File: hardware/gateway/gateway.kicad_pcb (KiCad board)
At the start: 2 copper layers, 65 x 32 mm, 29 parts, among them J1 FTDI, J2 Conn_Coaxial, J3 Raspberry_Pi_2_3, U1 RFM69HW, U2 MCP7940N-xSN, Y1 32768 - 6pF

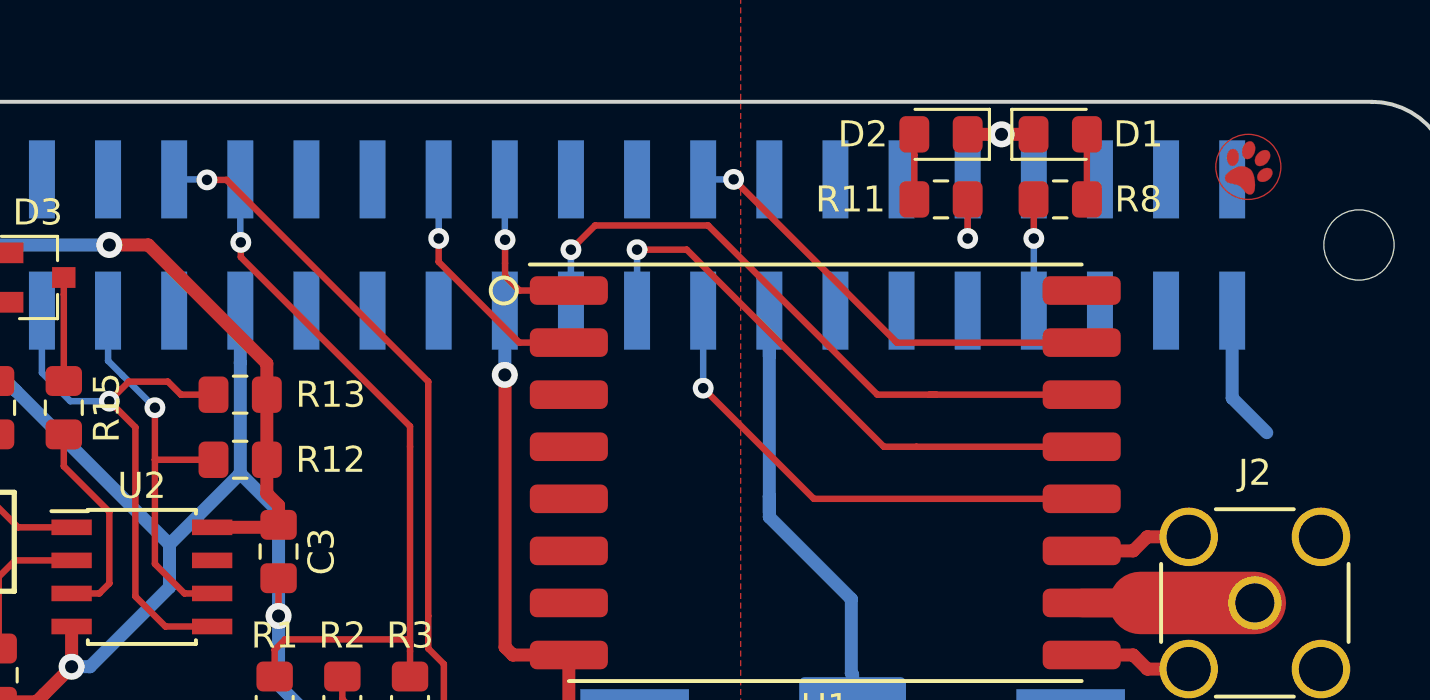
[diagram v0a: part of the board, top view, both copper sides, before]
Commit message: Added some silkscreen
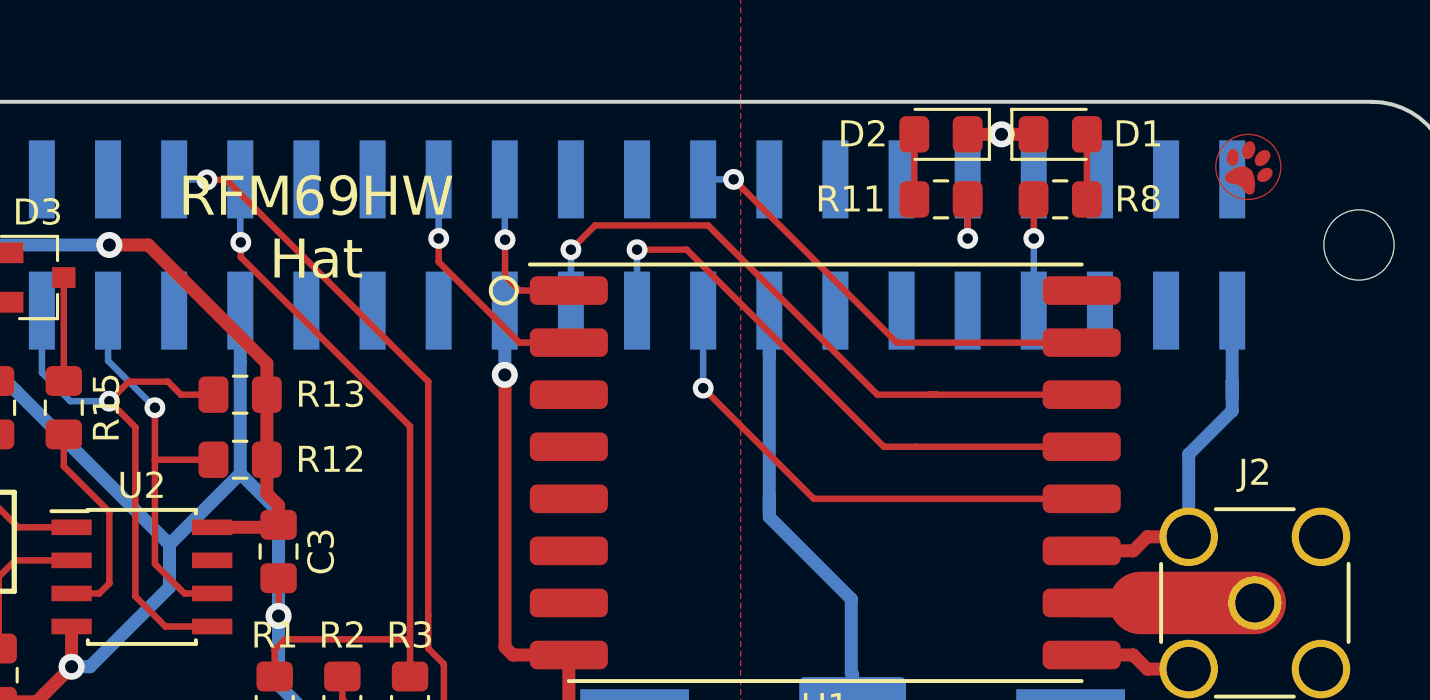
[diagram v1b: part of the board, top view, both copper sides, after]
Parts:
- added G***: LOGO, humidity:paw-large-screen-circ, B.Cu at (113.0, 63.2)
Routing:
- net GND: track 108.5 -> 113.3 mm
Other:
- board text added: "OOS 2019-06-13"
- board text added: "RFM69HW Hat"
- board text added: "Rev A"

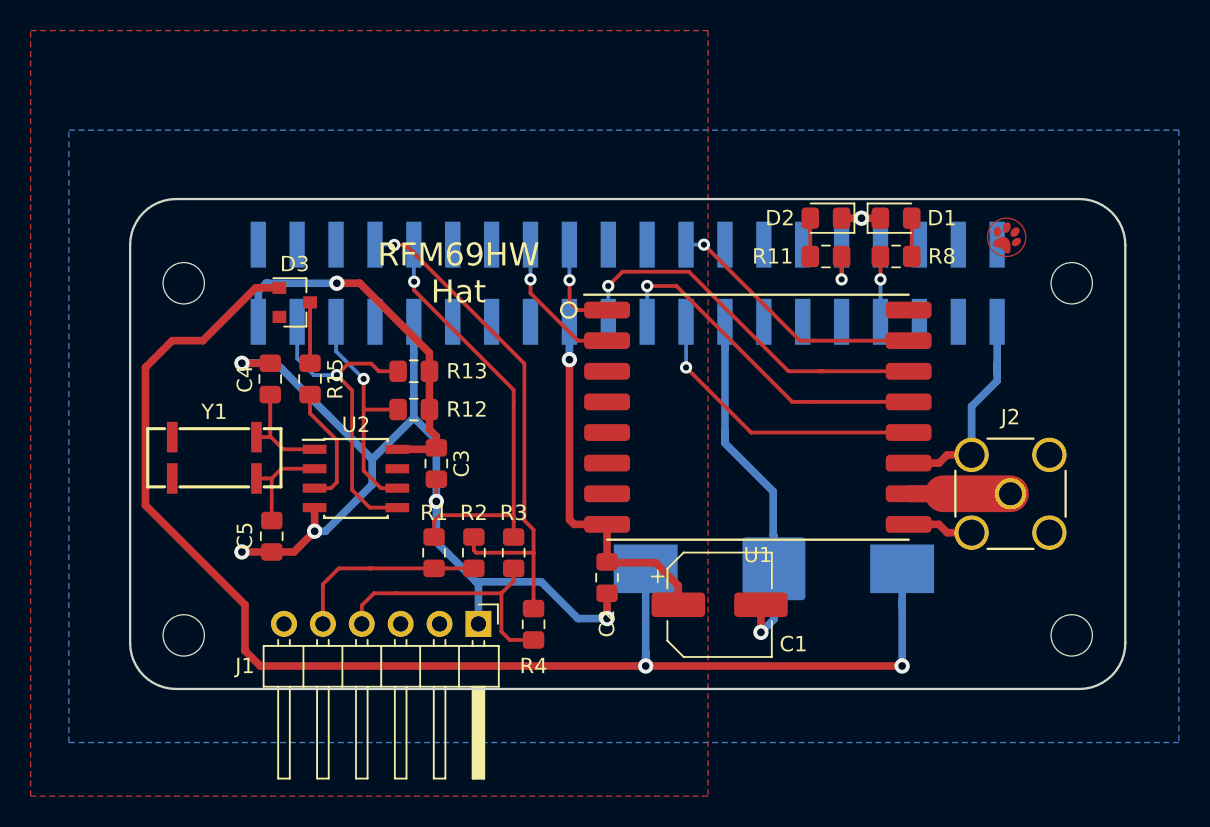
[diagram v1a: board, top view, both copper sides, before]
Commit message: Added local 3V3 regulator
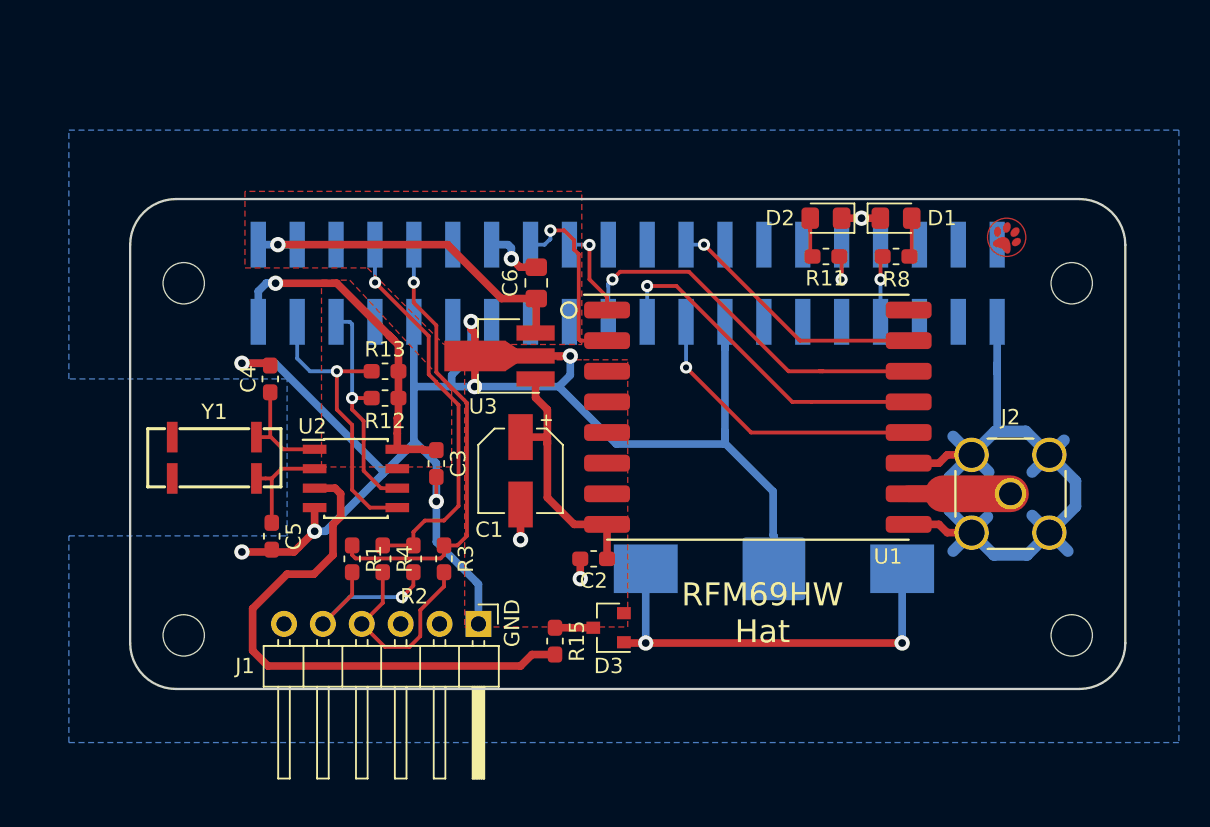
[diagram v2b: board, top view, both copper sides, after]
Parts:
- added C6: 1u, Capacitor_SMD:C_0805_2012Metric_Pad1.15x1.40mm_HandSolder, F.Cu at (123.0, 50.0)
- added U3: AP130-xxY, Package_TO_SOT_SMD:SOT-89-3_Handsoldering, F.Cu at (121.0, 54.8)
- C1: value 100u -> 22u; footprint Capacitor_SMD:CP_Elec_6.3x5.7 -> Capacitor_SMD:CP_Elec_5x5.3
- C2, C3, C4, C5: footprint Capacitor_SMD:C_0805_2012Metric_Pad1.15x1.40mm_HandSolder -> Capacitor_SMD:C_0603_1608Metric_Pad1.05x0.95mm_HandSolder
- R1, R12, R13, R4: footprint Resistor_SMD:R_0805_2012Metric_Pad1.15x1.40mm_HandSolder -> humidity:R_0603_1608Metric_Pad1.05x0.95mm_HandSolder-DNP
- R11, R15, R2, R3, R8: footprint Resistor_SMD:R_0805_2012Metric_Pad1.15x1.40mm_HandSolder -> Resistor_SMD:R_0603_1608Metric_Pad1.05x0.95mm_HandSolder
- moved D3 29.5 mm to (127.8, 72.5), turned to 180 degrees
- moved R15 23.4 mm to (124.2, 73.4)
- moved C1 15.7 mm to (122.0, 62.2), turned to 270 degrees
- moved R4 10.7 mm to (113.0, 68.0)
- moved G*** 5.63 mm to (118.5, 62.2)
- moved R1 5.36 mm to (111.0, 68.0)
- moved R3 4.57 mm to (117.0, 68.0)
- moved R2 3.97 mm to (115.0, 68.0)
- moved R12 2.02 mm to (113.2, 57.5)
- moved R13 1.88 mm to (113.2, 55.8)
- moved C2 1.51 mm to (126.8, 68.0), turned to 180 degrees
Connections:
- C1 pad 1: +3V3 -> +3V3_REG
- C2 pad 1: +3V3 -> +3V3_REG
- C3 pad 1: +3V3 -> +3V3_PI
- J3 pad 1: +3V3 -> +3V3_PI
- J3 pad 17: +3V3 -> Net-(J3-Pad17)
- J3 pad 2: Net-(J3-Pad2) -> +5V_PI
- J3 pad 4: Net-(J3-Pad4) -> +5V_PI
- R12 pad 2: +3V3 -> +3V3_PI
- R13 pad 2: +3V3 -> +3V3_PI
- U1 pad 8: +3V3 -> +3V3_REG
- U2 pad 8: +3V3 -> +3V3_PI
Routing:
- net GND: track 113.3 -> 179.5 mm, vias 7 -> 11
- net /VBAT_IN: track 89.4 -> 27.9 mm
- net +3V3: track 53.4 -> 0.00 mm, vias 2 -> 0
- net /VBAT: track 8.06 -> 36.0 mm
- net +5V_PI: track 0.00 -> 23.2 mm, vias 0 -> 1
- net +3V3_PI: track 0.00 -> 23.1 mm, vias 0 -> 1
- net +3V3_REG: track 0.00 -> 17.0 mm
- net /PI_TX: track 34.1 -> 25.9 mm
- net /FTDI_TX: track 17.4 -> 13.5 mm
- net /RFM_INT: track 9.45 -> 12.3 mm
- net /SDA: track 21.3 -> 19.3 mm
- net /PI_RX: track 28.1 -> 29.7 mm
- net /VBAT_D: track 3.98 -> 2.50 mm
- net /FTDI_RX: track 13.0 -> 12.0 mm, vias 0 -> 1
- added copper zone on F.Cu, net +3V3_PI
- added copper zone on F.Cu, net +3V3_REG
- added copper zone on F.Cu, net +5V_PI
- removed copper zone on F.Cu, net +3V3
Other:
- board text added: "GND"
- board text added: "RX"
- board text added: "TX"

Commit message: Layout improvemnets
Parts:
- added C7: 100n, Capacitor_SMD:C_0603_1608Metric_Pad1.05x0.95mm_HandSolder, F.Cu at (108.4, 68.8)
- added R5: 10k, Resistor_SMD:R_0603_1608Metric_Pad1.05x0.95mm_HandSolder, F.Cu at (114.2, 55.2)
- D3: value BAT54.215 -> B0520LW-7-F; footprint Package_TO_SOT_SMD:SOT-23 -> Diode_SMD:D_SOD-123
- moved C3 4.53 mm to (113.1, 58.8), turned to 180 degrees
- moved R13 3.94 mm to (109.6, 57.5)
- moved C2 3.87 mm to (123.6, 65.8)
- moved R12 3.83 mm to (109.6, 56.0)
- moved C1 1.46 mm to (121.2, 61.0), turned to 180 degrees
- moved C6 1.29 mm to (122.0, 50.8), turned to 180 degrees
- moved C4 1.28 mm to (105.4, 57.5), turned to 180 degrees
- moved R15 1.07 mm to (125.2, 73.0)
- moved C5 0.64 mm to (106.2, 66.1)
- moved D3 0.56 mm to (128.0, 73.0), turned to 270 degrees
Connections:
- net Net-(J3-Pad19) renamed /MOSI
- net Net-(J3-Pad21) renamed /MISO
- net Net-(J3-Pad23) renamed /SCK
- net Net-(J3-Pad24) renamed /CS
- D3 pad 1: /VBAT_IN -> /VBAT_D
- D3 pad 2: Net-(D3-Pad2) -> /VBAT_IN
- J3 pad 7: Net-(J3-Pad7) -> /MFP
- U2 pad 7: Net-(U2-Pad7) -> /MFP
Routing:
- net GND: track 179.5 -> 208.9 mm, vias 11 -> 13
- net /MFP: track 0.00 -> 12.9 mm, vias 0 -> 1
- net +5V_PI: track 23.2 -> 28.4 mm, vias 1 -> 2
- net +3V3_REG: track 17.0 -> 13.2 mm
- net +3V3_PI: track 23.1 -> 20.0 mm
- net /SDA: track 19.3 -> 16.5 mm
- net /PI_TX: track 25.9 -> 23.5 mm
- net /PI_RX: track 29.7 -> 27.9 mm
- net /VBAT: track 36.0 -> 37.7 mm
- net /VBAT_IN: track 27.9 -> 29.5 mm
- net /X1: track 6.90 -> 7.58 mm
- net /VBAT_D: track 2.50 -> 3.07 mm
- added copper zone on F.Cu, net GND

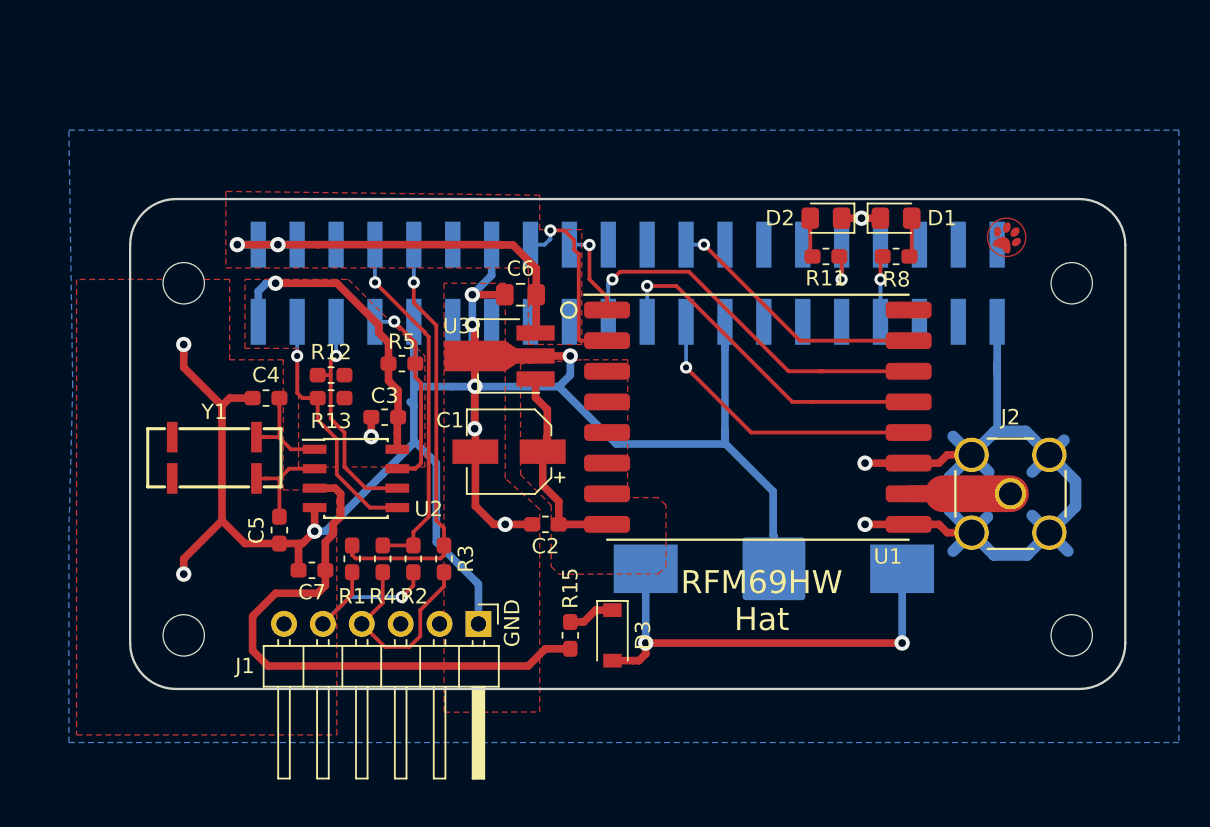
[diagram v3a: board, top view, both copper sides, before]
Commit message: Improved mounting holes and planes
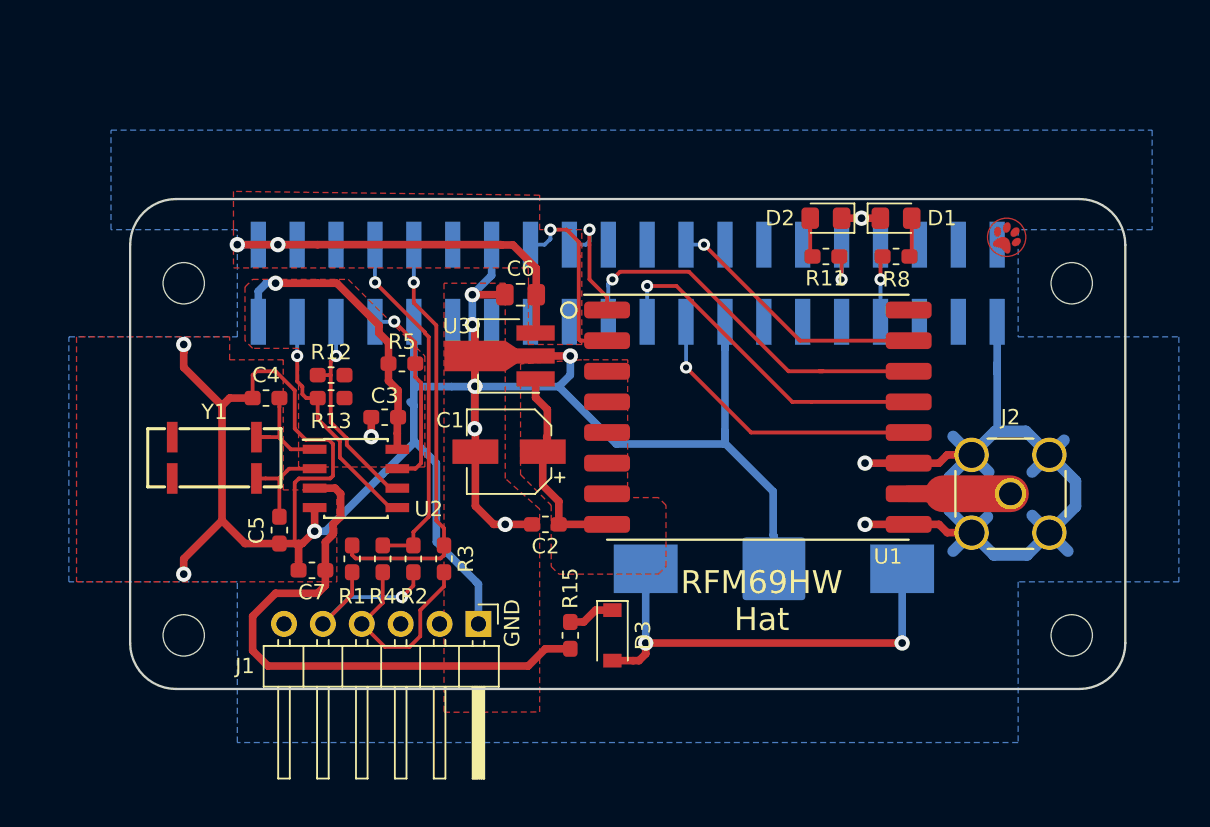
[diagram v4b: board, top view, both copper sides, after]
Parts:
- C4, C5: value C -> 10p
- D1: value LED -> KP-2012LSURCK
- D2: value LED -> KP-2012LSGC
- H1, H2, H3, H4: footprint MountingHole:MountingHole_2.7mm_M2.5 -> humidity:MountingHole_2.7mm_M2.5
- R11, R8: value 470 -> 330R
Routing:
- net GND: track 208.9 -> 227.9 mm
- net /RFM_RESET: track 6.04 -> 7.88 mm
- net /SCL: track 14.9 -> 14.0 mm
- net /SDA: track 16.5 -> 15.6 mm

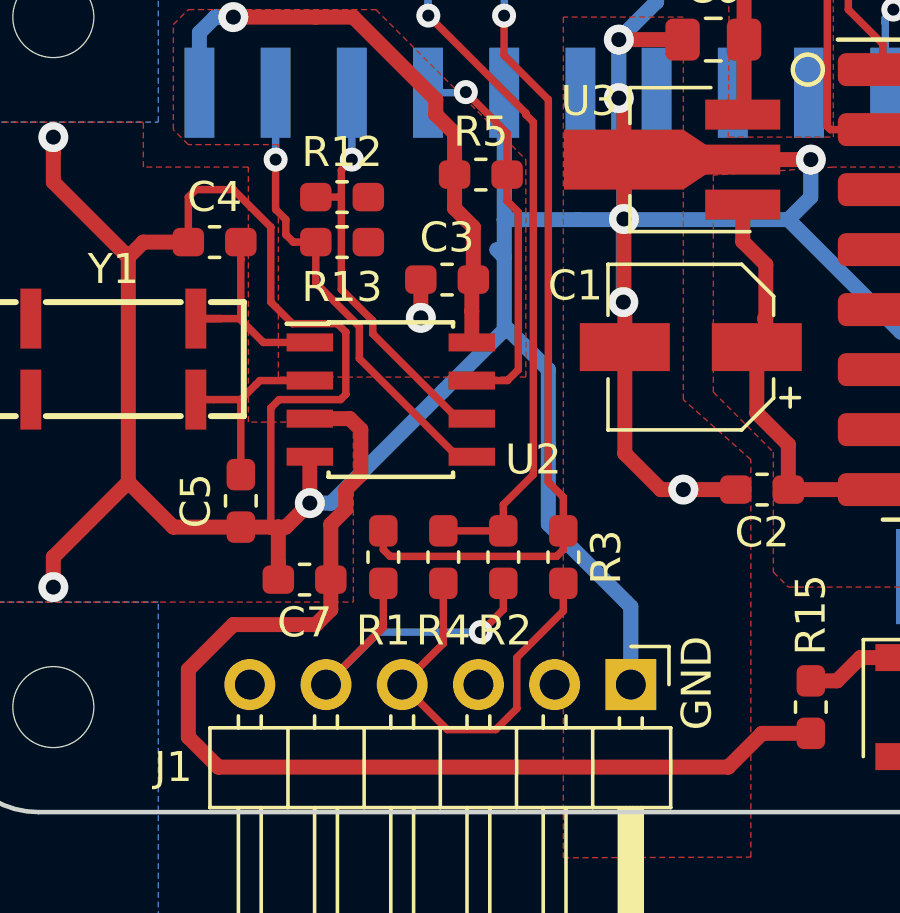
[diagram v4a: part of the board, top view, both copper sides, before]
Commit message: Improved optional resistors
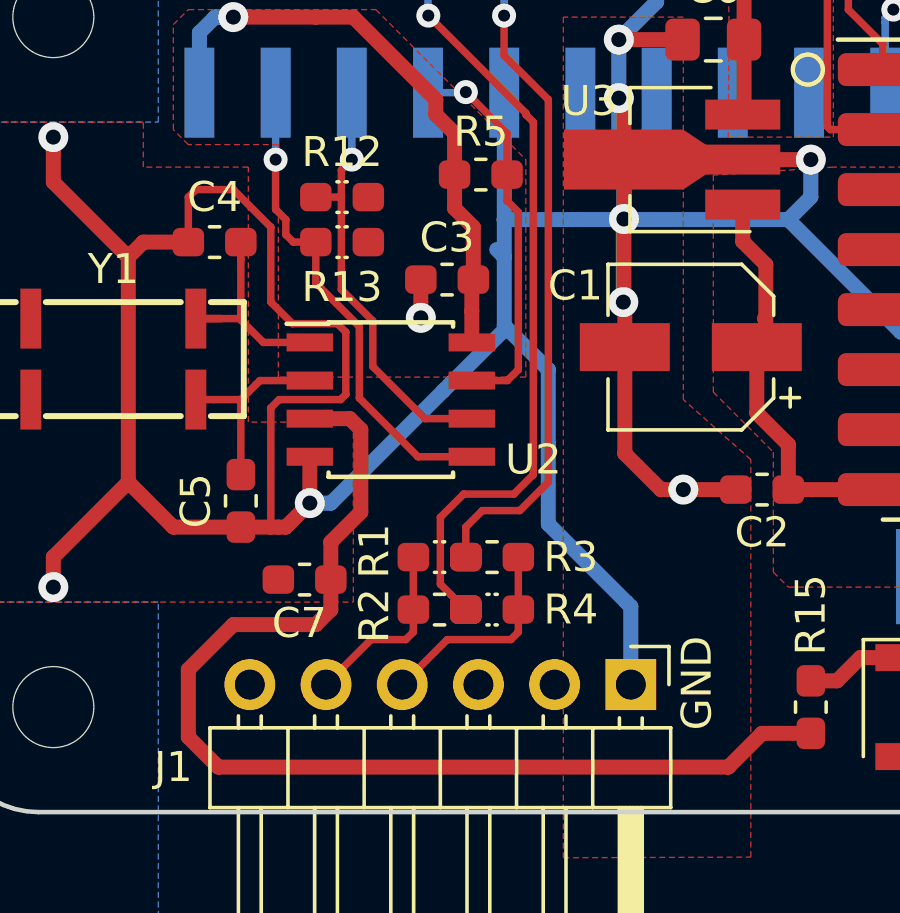
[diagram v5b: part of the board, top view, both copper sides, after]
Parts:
- moved R2 2.75 mm to (112.9, 69.8), turned to 180 degrees
- moved R4 2.39 mm to (114.6, 69.8), turned to 0 degrees
- moved R3 2.38 mm to (114.6, 68.0), turned to 0 degrees
- moved R1 1.88 mm to (112.9, 68.0), turned to 180 degrees
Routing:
- net /FTDI_TX: track 13.5 -> 7.09 mm
- net /FTDI_RX: track 12.0 -> 6.13 mm, vias 1 -> 0
- net /PI_RX: track 27.9 -> 23.0 mm
- net /PI_TX: track 23.5 -> 26.3 mm
- net GND: track 227.9 -> 226.1 mm
- net /SDA: track 15.6 -> 16.3 mm
- net /SCL: track 14.0 -> 14.6 mm
